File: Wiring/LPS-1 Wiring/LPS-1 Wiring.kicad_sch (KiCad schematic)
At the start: 9 parts, among them J1 +12V Connector block, J2 Battery, J4 Solar charging unit, J5 Solar Panel, J6 GND Connector Block], J7 LPS-1 Monitoring Unit, J8 Fuse Block, SW2 Load Monitoring Control, SW3 Battery Kill Switch

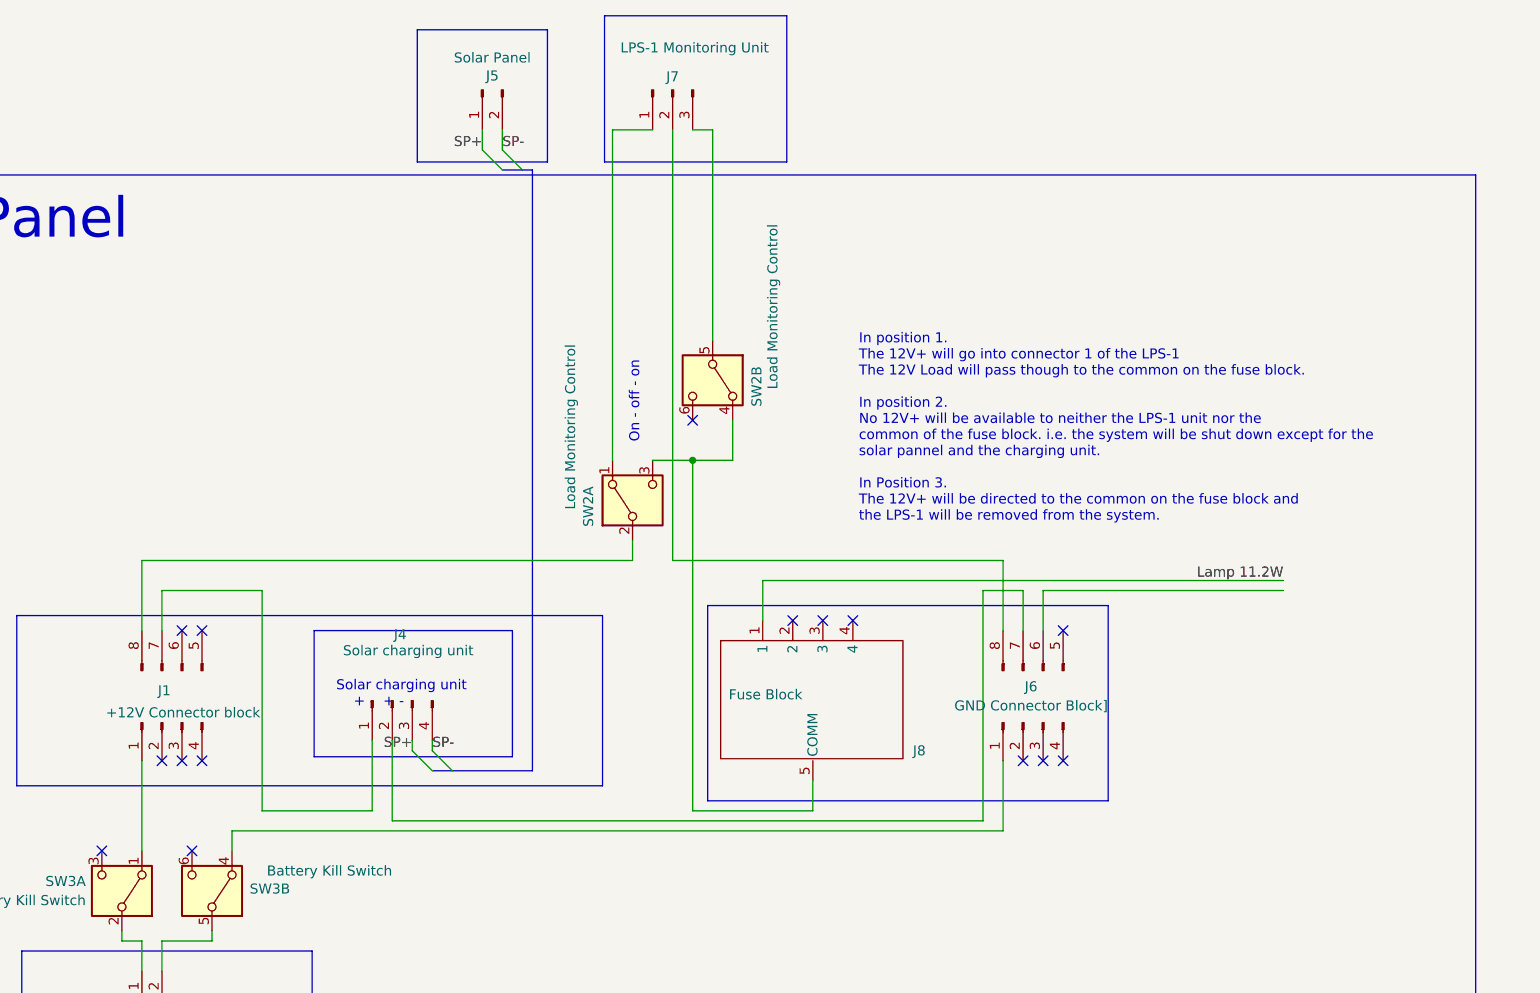
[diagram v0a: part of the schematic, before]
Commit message: Moved the design to KiCad 10
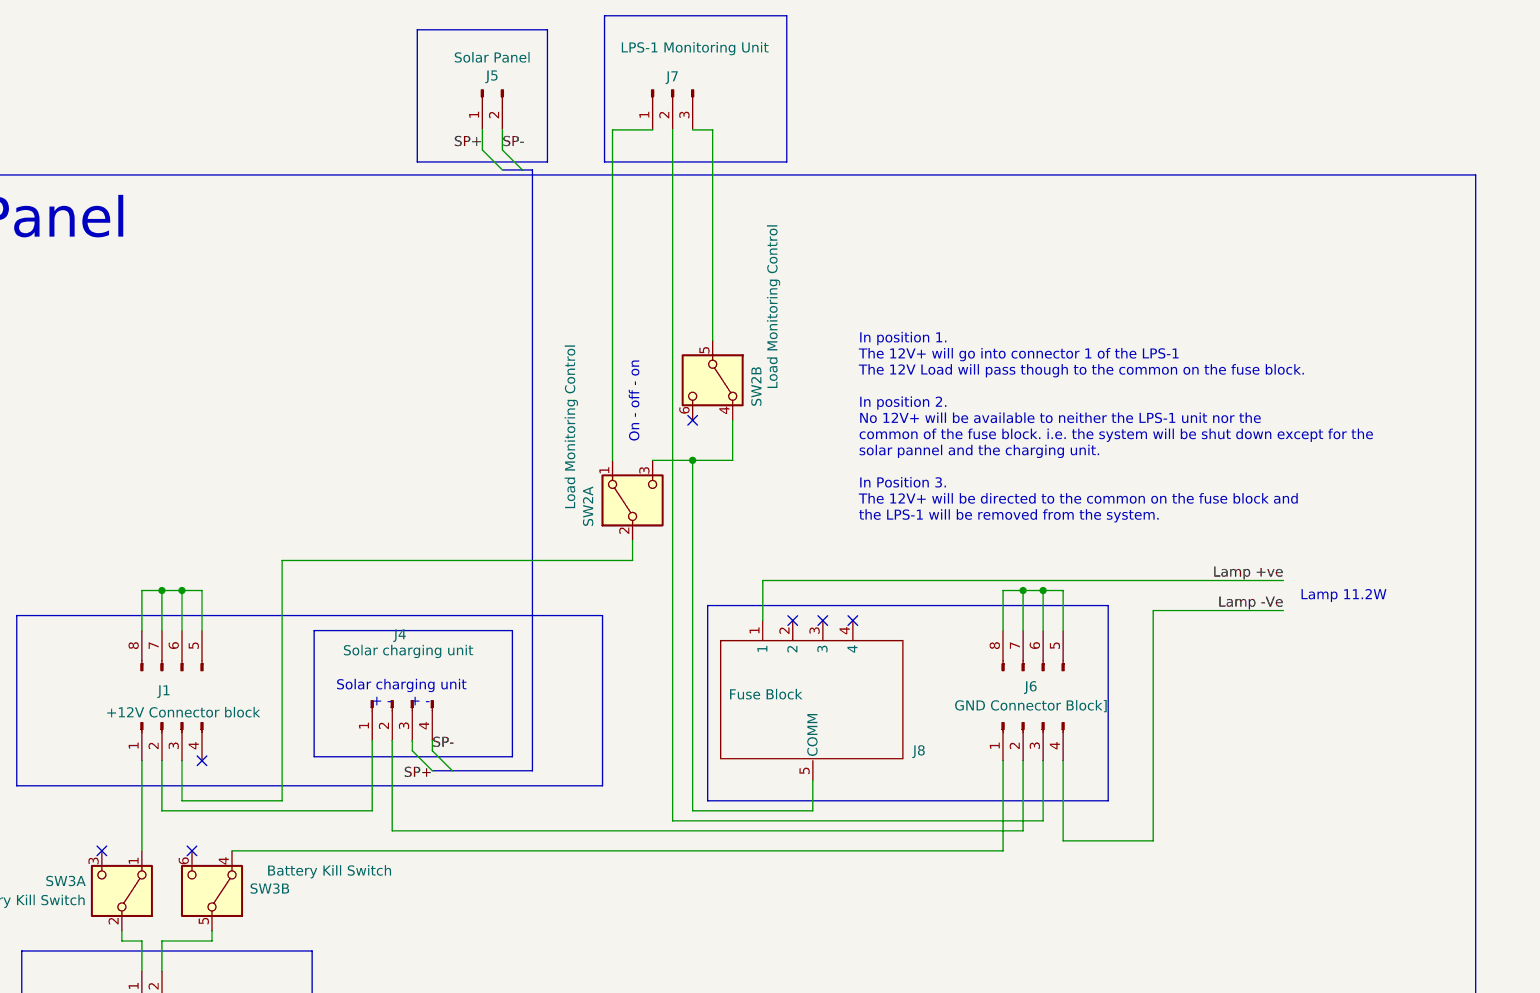
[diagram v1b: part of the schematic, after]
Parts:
- J1, J6: footprint Wiring:Degson_04_Bridged-PC2.5-01P-11-00AH-1_5.2 -> Wiring:Degson_04_Bridged-PC2.5-01P-11-00AH-1_5.2_H
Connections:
- net SP+: no longer J4.3 (Pin_3)
- net at SW2.2 (B): now also J1.3 (Pin_1); no longer J1.8 (Pin_2)
- net at J4.1 (Pin_1): now also J1.2 (Pin_2); no longer J1.7 (Pin_1)
- net at J4.2 (Pin_2): now also J6.2 (Pin_2); no longer J6.7 (Pin_1)
- net at J7.2 (Pin_2): now also J6.3 (Pin_1); no longer J6.8 (Pin_2)
- net Lamp -Ve: now reaches J6.4 (Pin_2)
- net at J6.5 (Pin_1): now also J6.6 (Pin_2), J6.7 (Pin_1), J6.8 (Pin_2)
- net at J1.5 (Pin_1): now also J1.6 (Pin_2), J1.7 (Pin_1), J1.8 (Pin_2)
- net Lamp 11.2W renamed Lamp +ve
- no-connect marks 15 -> 7
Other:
- note added: "Lamp 11.2W"

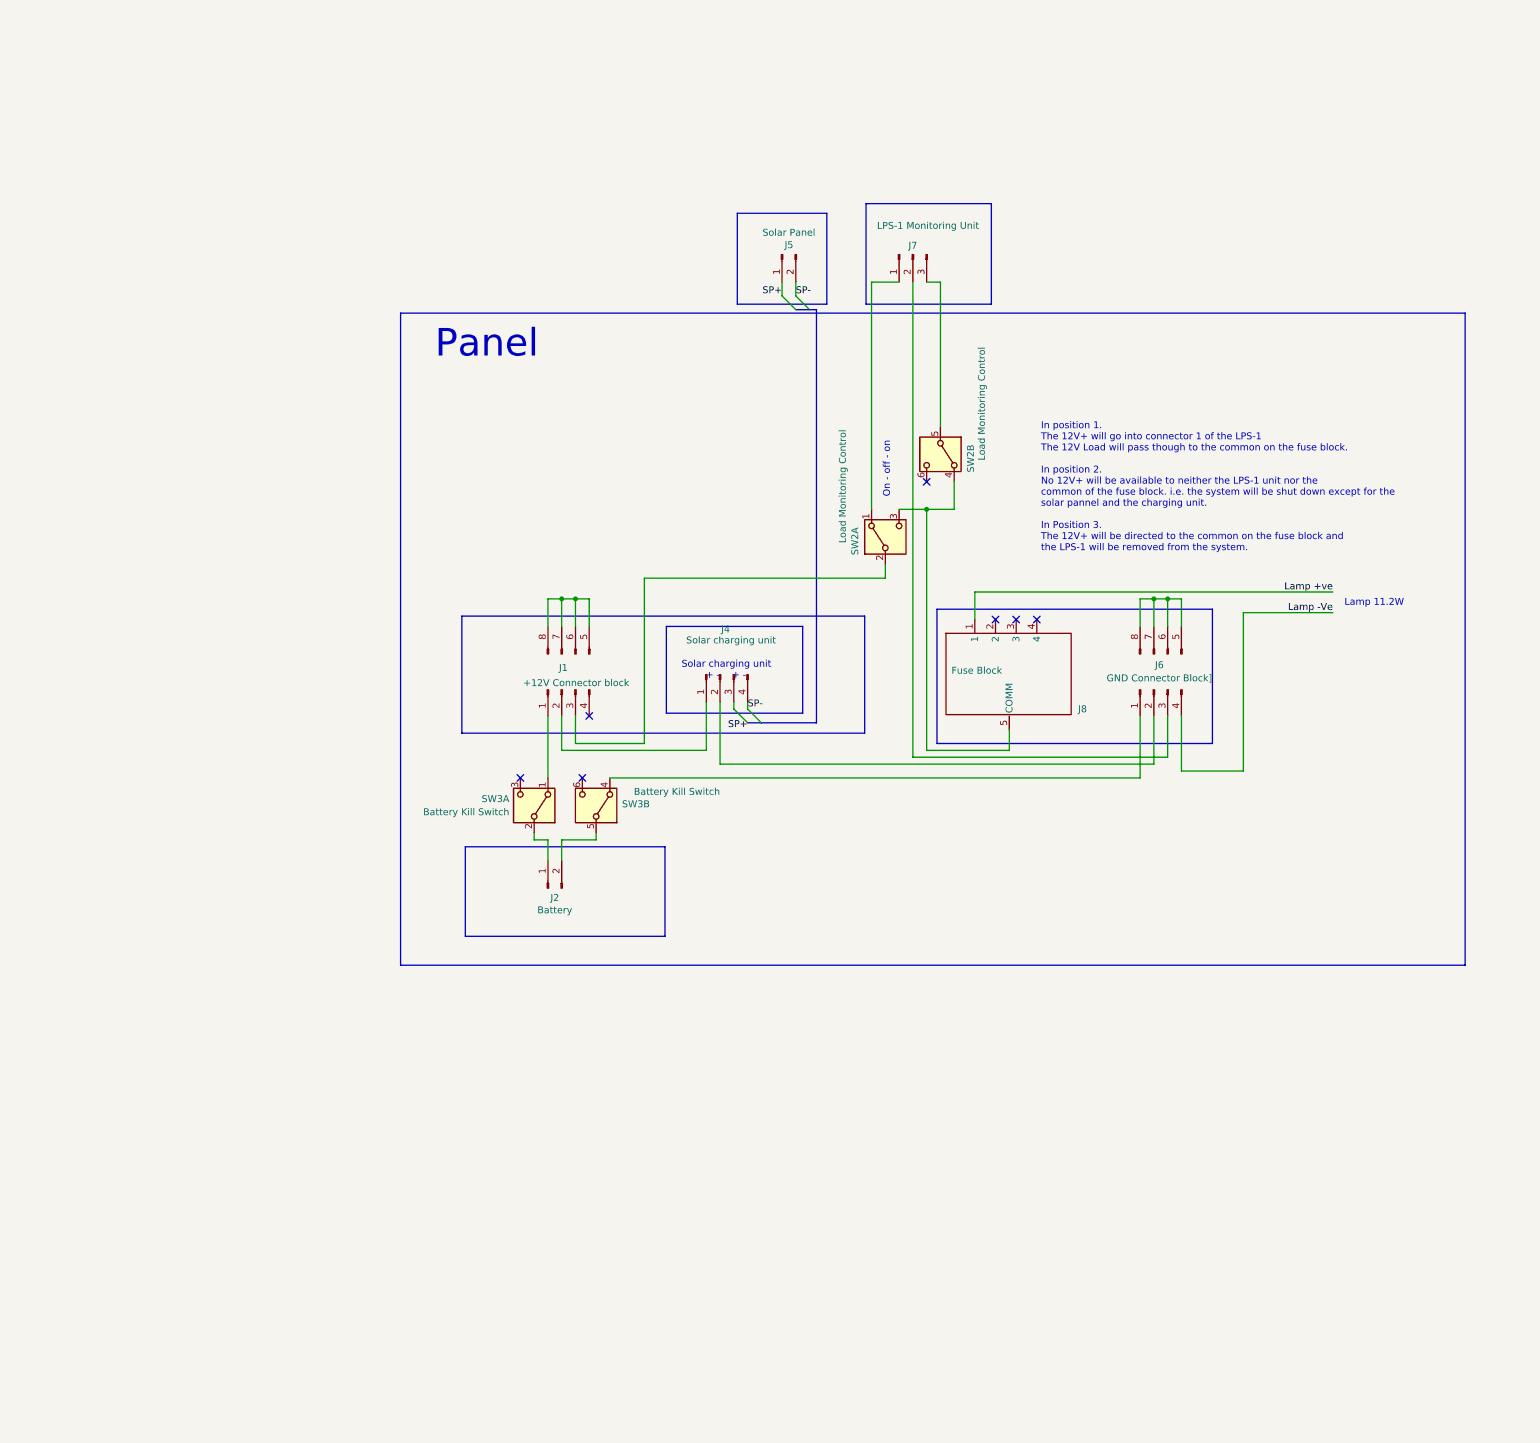
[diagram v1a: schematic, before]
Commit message: Update to the connection block symols and footprints
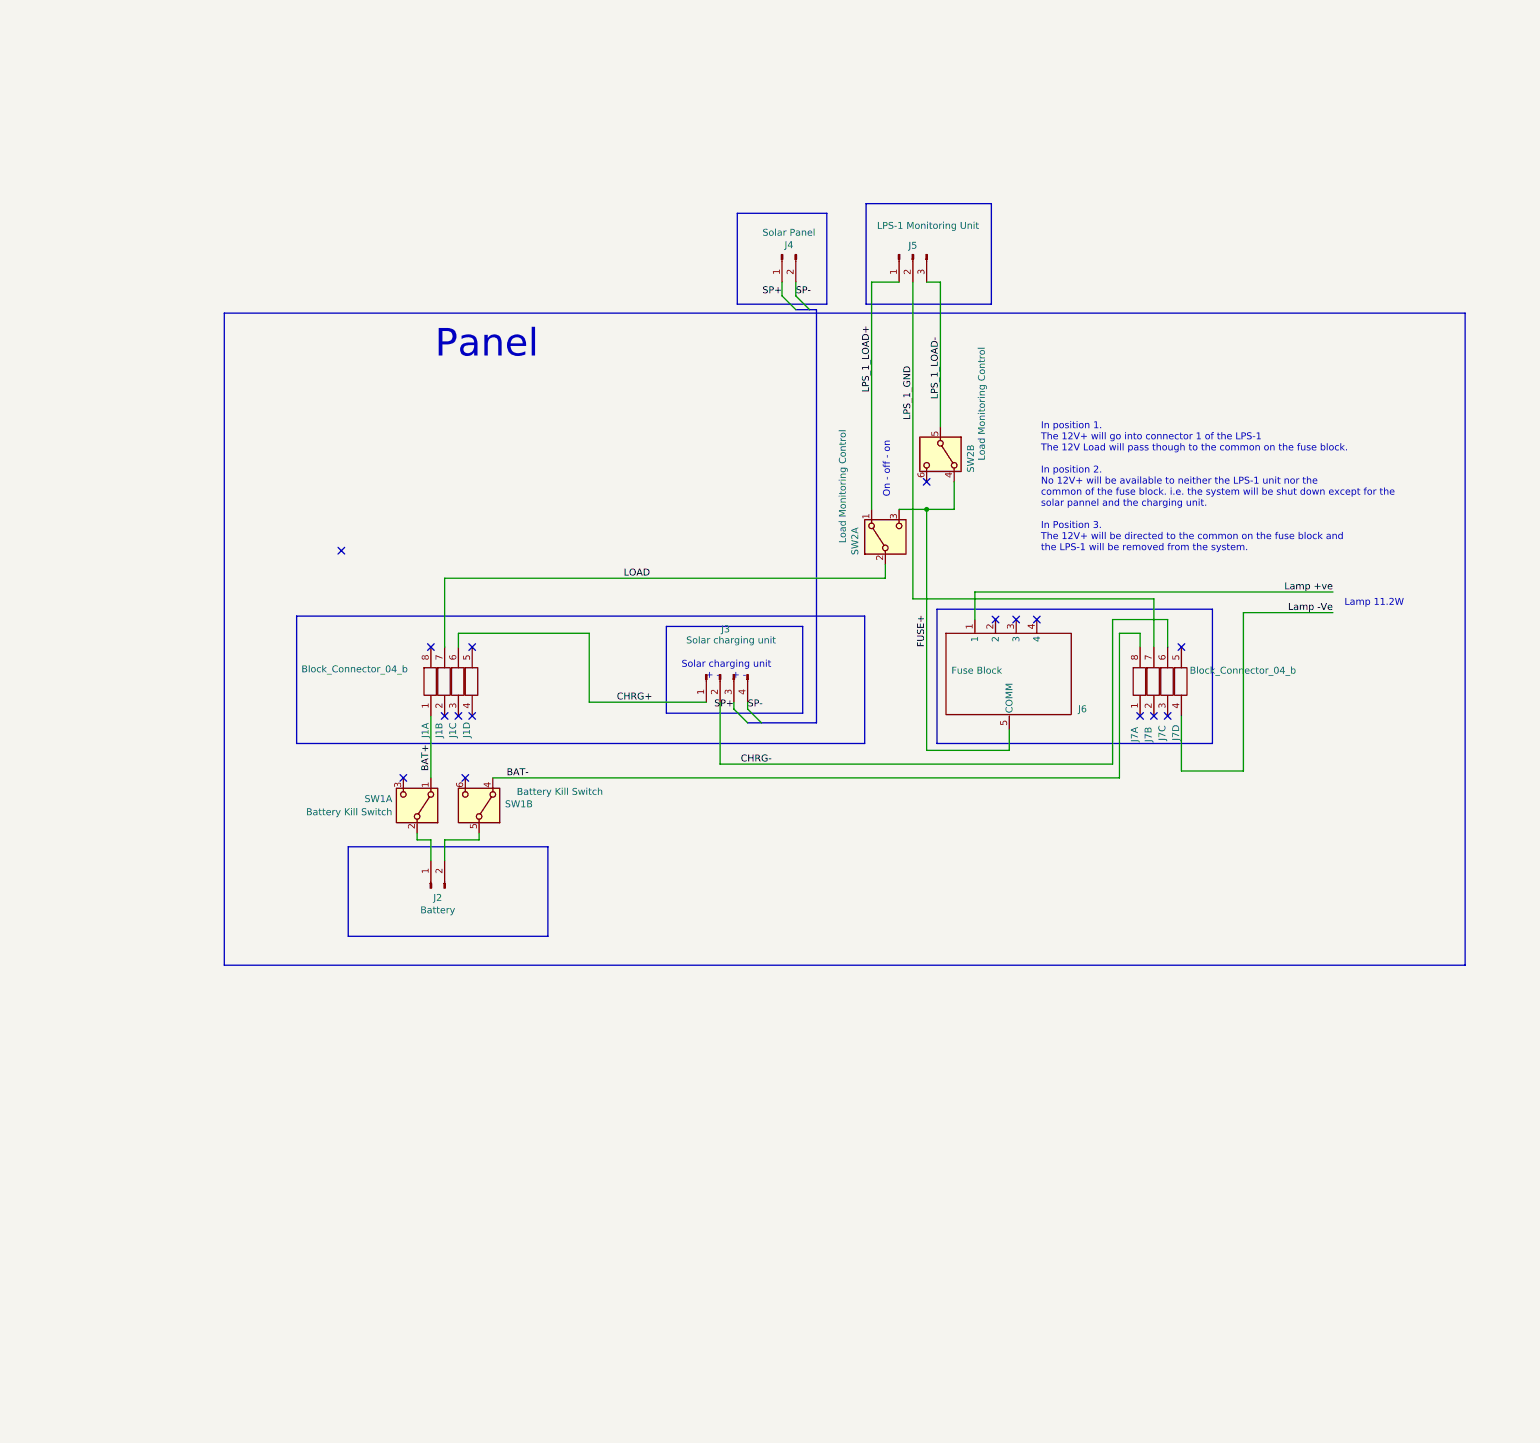
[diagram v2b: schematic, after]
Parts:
- removed J1: +12V Connector block, Wiring:Degson_04_Bridged-PC2.5-01P-11-00AH-1_5.2_H, symbol Wiring:Conn_01x04_Pin
- removed J6: GND Connector Block], Wiring:Degson_04_Bridged-PC2.5-01P-11-00AH-1_5.2_H, symbol Wiring:Conn_01x04_Pin
- added J1, J7: Block_Connector_04_b, Wiring:Degson_04_Bridged-PC2.5-01P-11-00AH-1_5.2, symbol Wiring:Block_Connector_04_Pin_B
- renumbered J4 to J3, J5 to J4, J7 to J5, J8 to J6, SW3 to SW1
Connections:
- net Lamp -Ve: now also J7.4
- net SP+: now also J3.3 (Pin_3)
- net BAT+: now reaches SW1.1 (A)
- net BAT+: now also J1.1
- net LPS_1_LOAD+: now reaches J5.1 (Pin_1), SW2.1 (A)
- net LOAD: now reaches SW2.2 (B)
- net LOAD: now also J1.7
- net FUSE+: now reaches J6.5 (COMM), SW2.3 (C), SW2.4 (A)
- net LPS_1_LOAD-: now reaches J5.3 (Pin_3), SW2.5 (B)
- net CHRG+: now reaches J3.1 (Pin_1)
- net CHRG+: now also J1.6
- net CHRG-: now reaches J3.2 (Pin_2)
- net CHRG-: now also J7.6
- net BAT-: now reaches SW1.4 (A)
- net BAT-: now also J7.8
- net LPS_1_GND: now reaches J5.2 (Pin_2)
- net LPS_1_GND: now also J7.7
- no-connect marks 7 -> 16
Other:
- moved on the sheet: J2, SW1A, SW1B
